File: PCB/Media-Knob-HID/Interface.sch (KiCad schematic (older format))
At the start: 52 parts, among them IC501 TS3USB30E, J501 USB_C_Buchse_SMD, J502 USB_C_Buchse_SMD, J503 USB_C_Buchse_SMD, J504 USB_C_Buchse_SMD, J505 USB_C_Buchse_SMD, J506 USB_C_Buchse_SMD, J507 USB_C_Buchse_SMD, J508 USB_C_Buchse_SMD

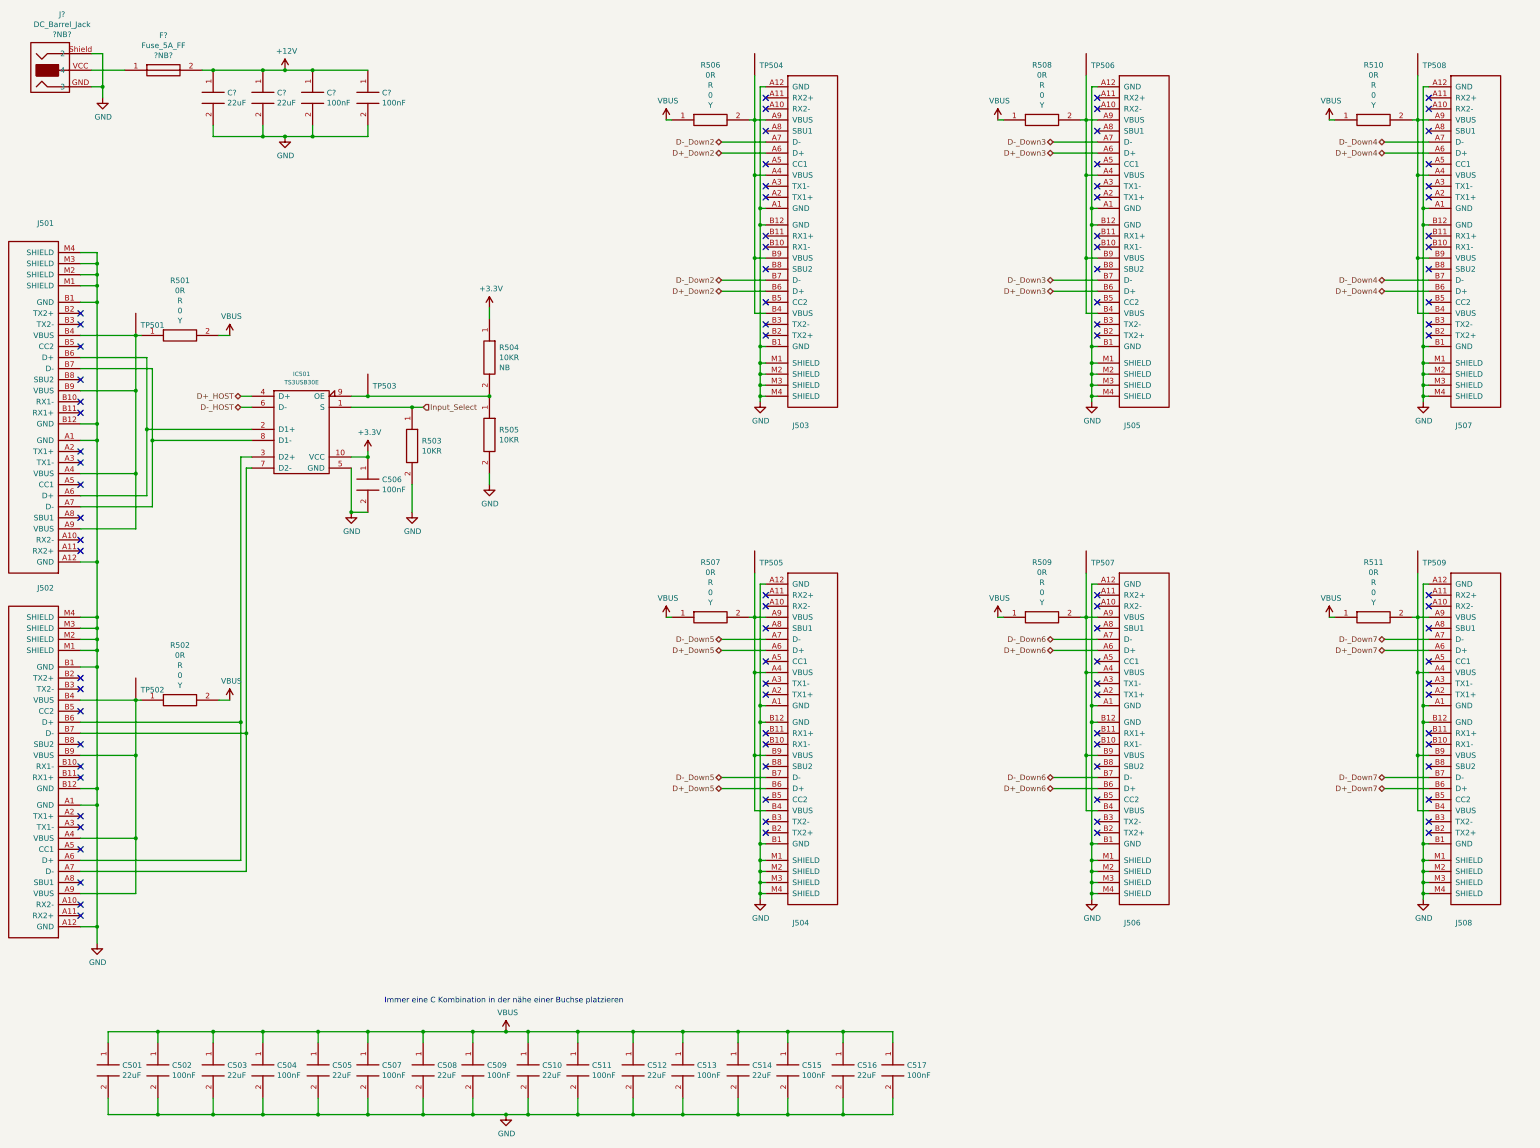
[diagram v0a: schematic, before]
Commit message: Grafik aktualisiert und zusätzliche USB Ports eingefügt
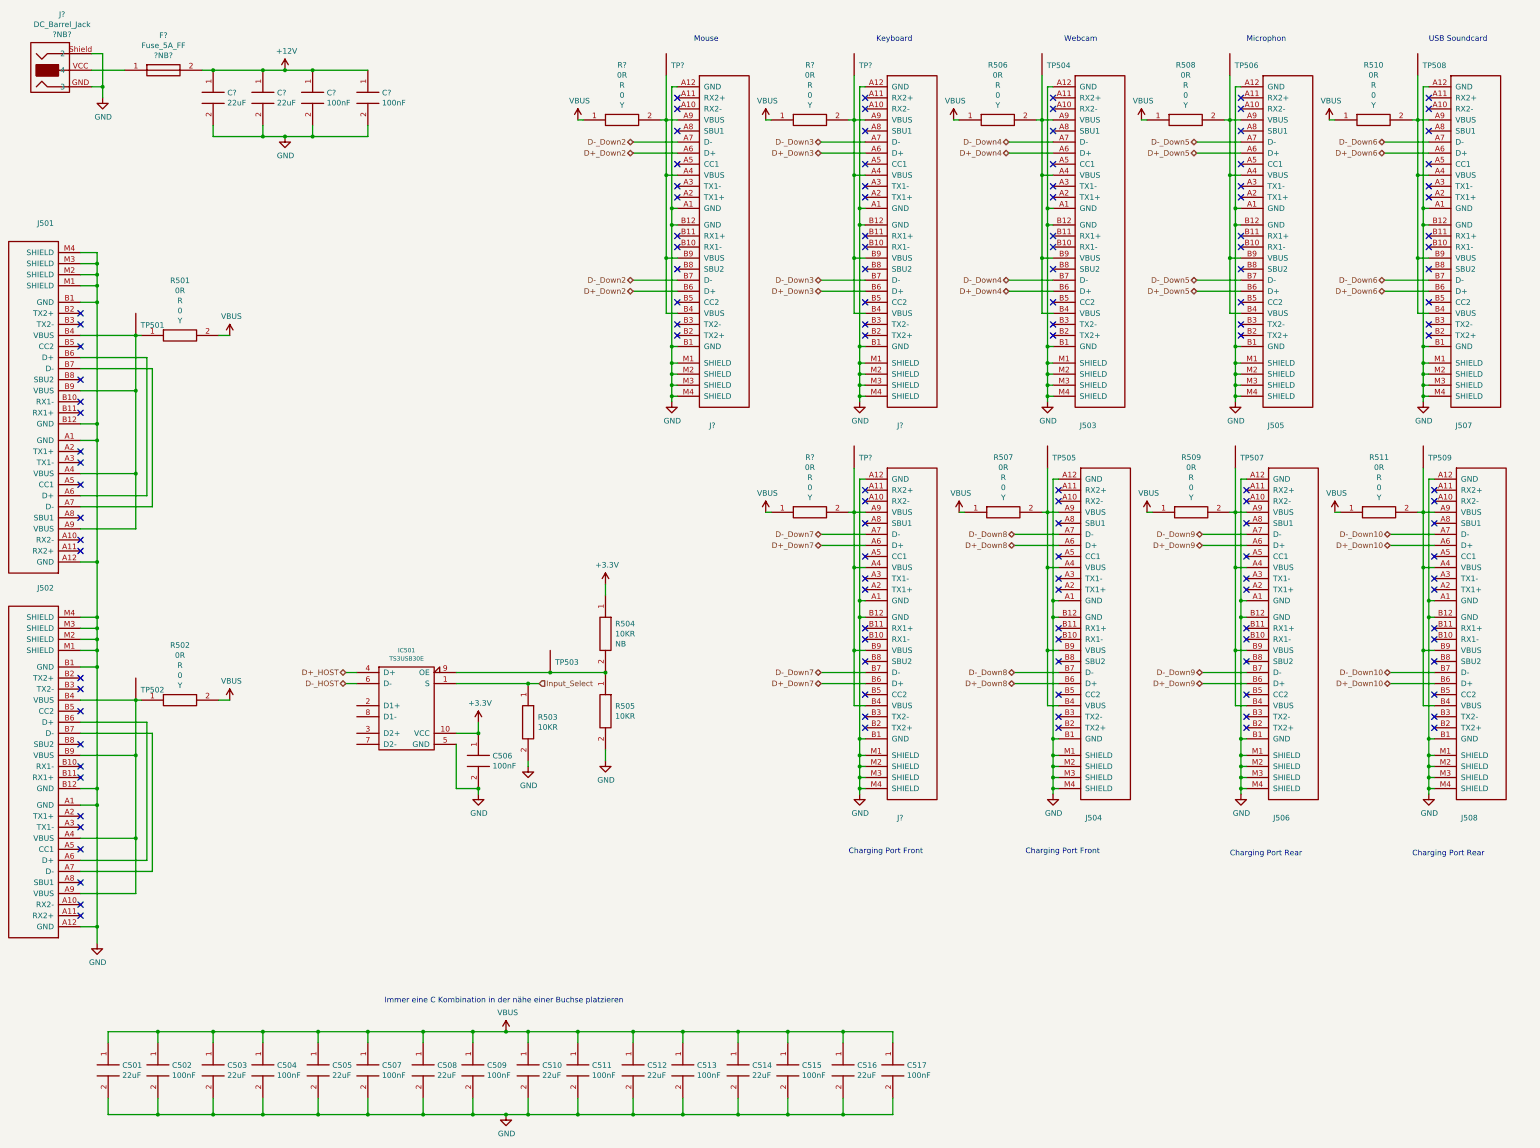
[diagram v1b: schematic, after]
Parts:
- added J? (x3): USB_C_Buchse_SMD, Stecker:USB_C_Buchse_SMD, symbol Stecker:USB_C_Buchse_SMD
- added R? (x3): 0R_0603, Widerstand:RESC1608, symbol Widerstand:0R_0603
- added TP? (x3): TP_100, Technik:TP100;, symbol Technik:TP_100
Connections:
- net D+_Down2: now also J?.A6 (D+), J?.B6 (D+); no longer J503.A6 (D+), J503.B6 (D+)
- net D+_Down3: now also J?.A6 (D+), J?.B6 (D+); no longer J505.A6 (D+), J505.B6 (D+)
- net D+_Down4: now also J503.A6 (D+), J503.B6 (D+); no longer J507.A6 (D+), J507.B6 (D+)
- net D+_Down5: now also J505.A6 (D+), J505.B6 (D+); no longer J504.A6 (D+), J504.B6 (D+)
- net D+_Down6: now also J507.A6 (D+), J507.B6 (D+); no longer J506.A6 (D+), J506.B6 (D+)
- net D+_Down7: now also J?.A6 (D+), J?.B6 (D+); no longer J508.A6 (D+), J508.B6 (D+)
- net D-_Down2: now also J?.A7 (D-), J?.B7 (D-); no longer J503.A7 (D-), J503.B7 (D-)
- net D-_Down3: now also J?.A7 (D-), J?.B7 (D-); no longer J505.A7 (D-), J505.B7 (D-)
- net D-_Down4: now also J503.A7 (D-), J503.B7 (D-); no longer J507.A7 (D-), J507.B7 (D-)
- net D-_Down5: now also J505.A7 (D-), J505.B7 (D-); no longer J504.A7 (D-), J504.B7 (D-)
- net D-_Down6: now also J507.A7 (D-), J507.B7 (D-); no longer J506.A7 (D-), J506.B7 (D-)
- net D-_Down7: now also J?.A7 (D-), J?.B7 (D-); no longer J508.A7 (D-), J508.B7 (D-)
- net GND: now also J?.A1 (GND), J?.A1 (GND), J?.A1 (GND), J?.A12 (GND), J?.A12 (GND), J?.A12 (GND), J?.B1 (GND), J?.B1 (GND), J?.B1 (GND), J?.B12 (GND), J?.B12 (GND), J?.B12 (GND), J?.M1 (SHIELD), J?.M1 (SHIELD), J?.M1 (SHIELD), J?.M2 (SHIELD), J?.M2 (SHIELD), J?.M2 (SHIELD), J?.M3 (SHIELD), J?.M3 (SHIELD), J?.M3 (SHIELD), J?.M4 (SHIELD), J?.M4 (SHIELD), J?.M4 (SHIELD)
- net VBUS: now also R?.1, R?.1, R?.1
- net at J501.A6 (D+), J501.B6 (D+): no longer IC501.2 (D1+)
- net at J501.A7 (D-), J501.B7 (D-): no longer IC501.8 (D1-)
- net at J502.A6 (D+), J502.B6 (D+): no longer IC501.3 (D2+)
- net at J502.A7 (D-), J502.B7 (D-): no longer IC501.7 (D2-)
- new net: J?.A4 (VBUS), J?.A9 (VBUS), J?.B4 (VBUS), J?.B9 (VBUS), R?.2, TP?.1 (x3)
- new net D+_Down10: J508.A6 (D+), J508.B6 (D+)
- new net D+_Down8: J504.A6 (D+), J504.B6 (D+)
- new net D+_Down9: J506.A6 (D+), J506.B6 (D+)
- new net D-_Down10: J508.A7 (D-), J508.B7 (D-)
- new net D-_Down8: J504.A7 (D-), J504.B7 (D-)
- new net D-_Down9: J506.A7 (D-), J506.B7 (D-)
- no-connect marks 96 -> 132
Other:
- note added: "Charging Port Front\n"
- note added: "Charging Port Rear\n\n"
- note added: "Keyboard\n"
- note added: "Microphon\n"
- note added: "Mouse\n"
- note added: "USB Soundcard\n"
- note added: "Webcam\n"
- moved on the sheet: C506, IC501, J503, J504, J505, J506, J508, R503, R504, R505, R506, R507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

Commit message: ESD Schutz eingefügt und Projekt vereinfacht
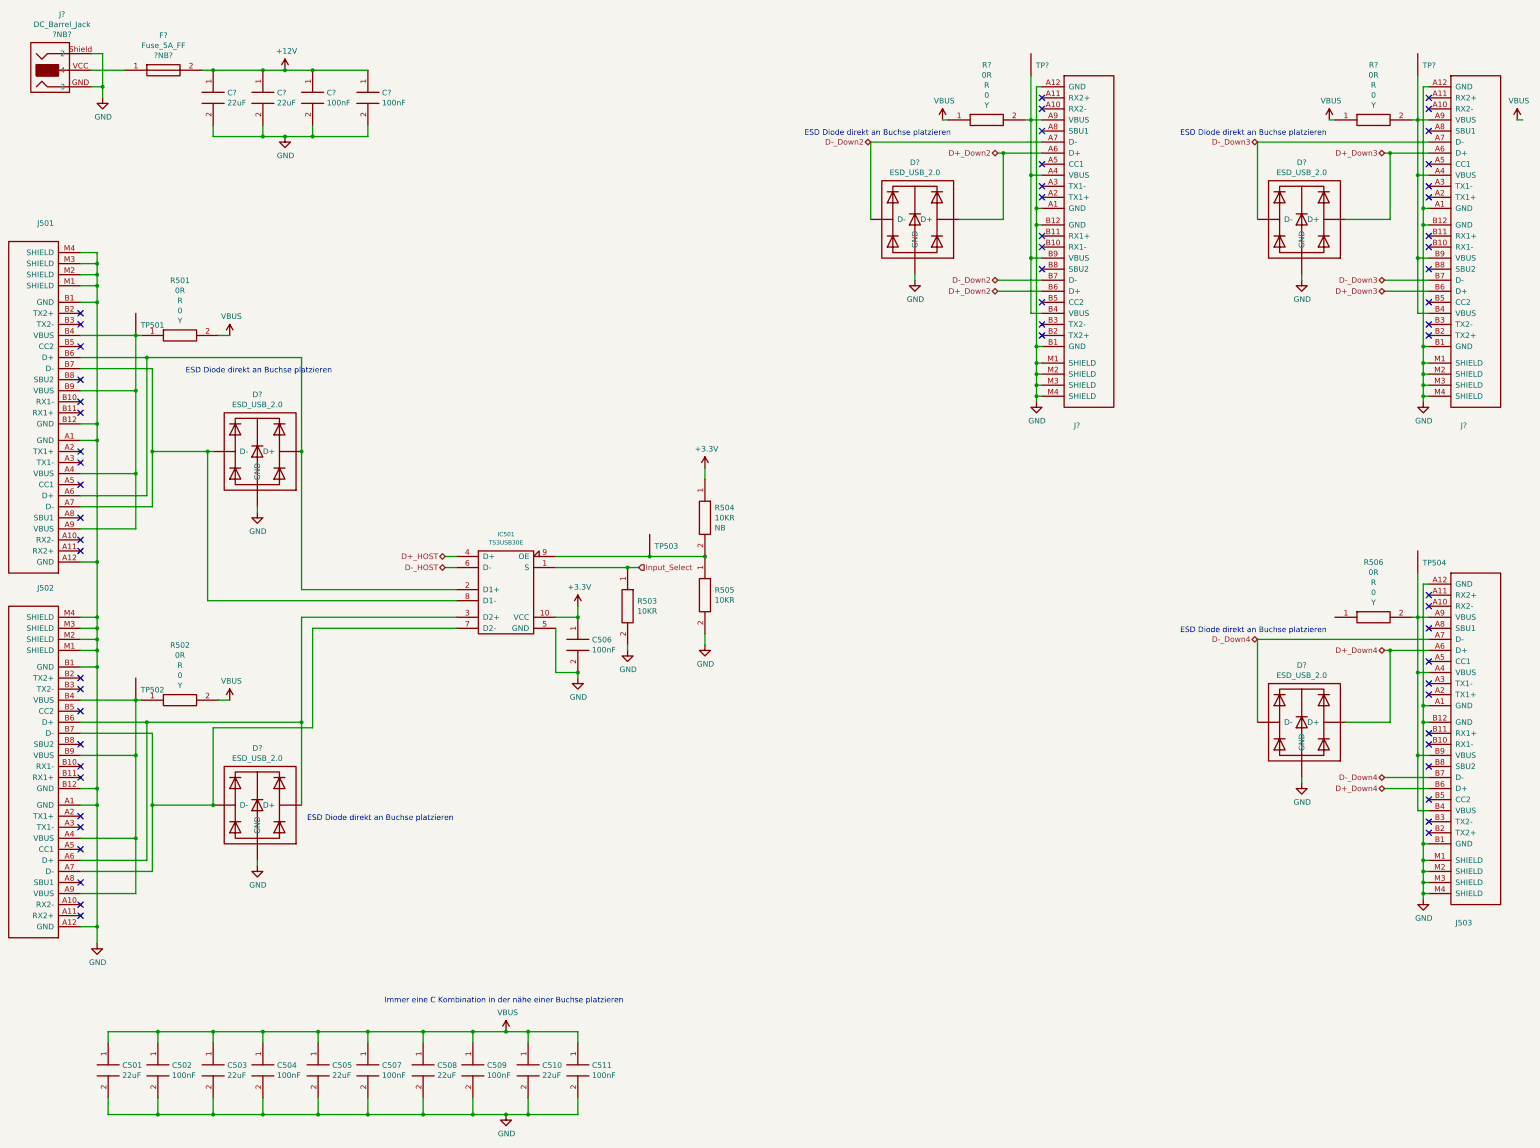
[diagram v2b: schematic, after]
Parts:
- removed C512, C514, C516: 22u_1210, Kondensator:CAPC3225, symbol Kondensator:22u_1210
- removed C513, C515, C517: 100n_0603, Kondensator:CAPC1608, symbol Kondensator:100n_0603
- removed J504, J505, J506, J507, J508, J?: USB_C_Buchse_SMD, Stecker:USB_C_Buchse_SMD, symbol Stecker:USB_C_Buchse_SMD
- removed R507, R508, R509, R510, R511, R?: 0R_0603, Widerstand:RESC1608, symbol Widerstand:0R_0603
- removed TP505, TP506, TP507, TP508, TP509, TP?: TP_100, Technik:TP100;, symbol Technik:TP_100
- added D? (x5): ESD_USB_2.0, symbol Artikel:ESD_USB_2.0
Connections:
- net D+_Down2: now also D?.~ (GND)
- net D+_Down3: now also D?.~ (GND)
- net D+_Down4: now also D?.~ (GND)
- net D-_Down2: now also D?.~ (GND)
- net D-_Down3: now also D?.~ (GND)
- net D-_Down4: now also D?.~ (GND)
- net GND: now also D?.~ (GND), D?.~ (GND), D?.~ (GND), D?.~ (GND), D?.~ (GND)
- net VBUS: no longer R506.1
- net at J501.A6 (D+), J501.B6 (D+): now also IC501.2 (D1+), D?.~ (GND)
- net at J501.A7 (D-), J501.B7 (D-): now also IC501.8 (D1-), D?.~ (GND)
- net at J502.A6 (D+), J502.B6 (D+): now also IC501.3 (D2+), D?.~ (GND)
- net at J502.A7 (D-), J502.B7 (D-): now also IC501.7 (D2-), D?.~ (GND)
- no-connect marks 132 -> 60
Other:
- note added: "ESD Diode direkt an Buchse platzieren\n"
- note removed: "Charging Port Front\n"
- note removed: "Charging Port Rear\n\n"
- note removed: "Keyboard\n"
- note removed: "Microphon\n"
- note removed: "Mouse\n"
- note removed: "USB Soundcard\n"
- note removed: "Webcam\n"
- moved on the sheet: C506, IC501, J503, J?, R503, R504, R505, R506, R?, TP503, TP504, TP?
